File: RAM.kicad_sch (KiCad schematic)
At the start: 26 parts

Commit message: update traces
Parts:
- B5, B8, C10, C3, C4, C5, C6, C7, C8, C9, D10, D3, D4, D5, D6, D7, D8, D9, E10, E3, E4, E5, E6, E7, E8, E9: footprint Apple:DIP-16_W7.62mm -> Package_DIP:DIP-16_W7.62mm
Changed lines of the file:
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@@
       (effects (font (size 1.27 1.27)))
     )
-    (property "Footprint" "Apple:DIP-16_W7.62mm" (at 157.48 44.196 0)
+    (property "Footprint" "Package_DIP:DIP-16_W7.62mm" (at 157.48 44.196 0)
       (effects (font (size 1.27 1.27)) hide)
     )
@@
       (effects (font (size 1.27 1.27)))
     )
-    (property "Footprint" "Apple:DIP-16_W7.62mm" (at 189.992 44.196 0)
+    (property "Footprint" "Package_DIP:DIP-16_W7.62mm" (at 189.992 44.196 0)
       (effects (font (size 1.27 1.27)) hide)
     )
@@
       (effects (font (size 1.27 1.27)))
     )
-    (property "Footprint" "Apple:DIP-16_W7.62mm" (at 221.996 44.196 0)
+    (property "Footprint" "Package_DIP:DIP-16_W7.62mm" (at 221.996 44.196 0)
       (effects (font (size 1.27 1.27)) hide)
     )
@@
       (effects (font (size 1.27 1.27)))
     )
-    (property "Footprint" "Apple:DIP-16_W7.62mm" (at 319.786 44.196 0)
+    (property "Footprint" "Package_DIP:DIP-16_W7.62mm" (at 319.786 44.196 0)
       (effects (font (size 1.27 1.27)) hide)
     )
@@
       (effects (font (size 1.27 1.27)))
     )
-    (property "Footprint" "Apple:DIP-16_W7.62mm" (at 157.734 91.44 0)
+    (property "Footprint" "Package_DIP:DIP-16_W7.62mm" (at 157.734 91.44 0)
       (effects (font (size 1.27 1.27)) hide)
     )
@@
       (effects (font (size 1.27 1.27)))
     )
-    (property "Footprint" "Apple:DIP-16_W7.62mm" (at 190.246 91.44 0)
+    (property "Footprint" "Package_DIP:DIP-16_W7.62mm" (at 190.246 91.44 0)
       (effects (font (size 1.27 1.27)) hide)
     )
@@
       (effects (font (size 1.27 1.27)))
     )
-    (property "Footprint" "Apple:DIP-16_W7.62mm" (at 222.25 91.44 0)
+    (property "Footprint" "Package_DIP:DIP-16_W7.62mm" (at 222.25 91.44 0)
       (effects (font (size 1.27 1.27)) hide)
     )
@@
       (effects (font (size 1.27 1.27)))
     )
-    (property "Footprint" "Apple:DIP-16_W7.62mm" (at 287.528 91.44 0)
+    (property "Footprint" "Package_DIP:DIP-16_W7.62mm" (at 287.528 91.44 0)
       (effects (font (size 1.27 1.27)) hide)
     )
@@
       (effects (font (size 1.27 1.27)))
     )
-    (property "Footprint" "Apple:DIP-16_W7.62mm" (at 352.044 91.44 0)
+    (property "Footprint" "Package_DIP:DIP-16_W7.62mm" (at 352.044 91.44 0)
       (effects (font (size 1.27 1.27)) hide)
     )
@@
       (effects (font (size 1.27 1.27)))
     )
-    (property "Footprint" "Apple:DIP-16_W7.62mm" (at 125.73 44.45 0)
+    (property "Footprint" "Package_DIP:DIP-16_W7.62mm" (at 125.73 44.45 0)
       (effects (font (size 1.27 1.27)) hide)
     )
@@
       (effects (font (size 1.27 1.27)))
     )
-    (property "Footprint" "Apple:DIP-16_W7.62mm" (at 255.27 44.196 0)
+    (property "Footprint" "Package_DIP:DIP-16_W7.62mm" (at 255.27 44.196 0)
       (effects (font (size 1.27 1.27)) hide)
     )
@@
       (effects (font (size 1.27 1.27)))
     )
-    (property "Footprint" "Apple:DIP-16_W7.62mm" (at 287.274 44.196 0)
+    (property "Footprint" "Package_DIP:DIP-16_W7.62mm" (at 287.274 44.196 0)
       (effects (font (size 1.27 1.27)) hide)
     )
@@
       (effects (font (size 1.27 1.27)))
     )
-    (property "Footprint" "Apple:DIP-16_W7.62mm" (at 351.79 44.196 0)
+    (property "Footprint" "Package_DIP:DIP-16_W7.62mm" (at 351.79 44.196 0)
       (effects (font (size 1.27 1.27)) hide)
     )
@@
       (effects (font (size 1.27 1.27)))
     )
-    (property "Footprint" "Apple:DIP-16_W7.62mm" (at 255.524 91.44 0)
+    (property "Footprint" "Package_DIP:DIP-16_W7.62mm" (at 255.524 91.44 0)
       (effects (font (size 1.27 1.27)) hide)
     )
@@
       (effects (font (size 1.27 1.27)))
     )
-    (property "Footprint" "Apple:DIP-16_W7.62mm" (at 320.04 91.44 0)
+    (property "Footprint" "Package_DIP:DIP-16_W7.62mm" (at 320.04 91.44 0)
       (effects (font (size 1.27 1.27)) hide)
     )
@@
       (effects (font (size 1.27 1.27)))
     )
-    (property "Footprint" "Apple:DIP-16_W7.62mm" (at 123.952 139.192 0)
+    (property "Footprint" "Package_DIP:DIP-16_W7.62mm" (at 123.952 139.192 0)
       (effects (font (size 1.27 1.27)) hide)
     )
@@
       (effects (font (size 1.27 1.27)))
     )
-    (property "Footprint" "Apple:DIP-16_W7.62mm" (at 155.956 139.192 0)
+    (property "Footprint" "Package_DIP:DIP-16_W7.62mm" (at 155.956 139.192 0)
       (effects (font (size 1.27 1.27)) hide)
     )
@@
       (effects (font (size 1.27 1.27)))
     )
-    (property "Footprint" "Apple:DIP-16_W7.62mm" (at 188.468 139.192 0)
+    (property "Footprint" "Package_DIP:DIP-16_W7.62mm" (at 188.468 139.192 0)
       (effects (font (size 1.27 1.27)) hide)
     )
@@
       (effects (font (size 1.27 1.27)))
     )
-    (property "Footprint" "Apple:DIP-16_W7.62mm" (at 220.472 139.192 0)
+    (property "Footprint" "Package_DIP:DIP-16_W7.62mm" (at 220.472 139.192 0)
       (effects (font (size 1.27 1.27)) hide)
     )
@@
       (effects (font (size 1.27 1.27)))
     )
-    (property "Footprint" "Apple:DIP-16_W7.62mm" (at 253.746 139.192 0)
+    (property "Footprint" "Package_DIP:DIP-16_W7.62mm" (at 253.746 139.192 0)
       (effects (font (size 1.27 1.27)) hide)
     )
@@
       (effects (font (size 1.27 1.27)))
     )
-    (property "Footprint" "Apple:DIP-16_W7.62mm" (at 285.75 139.192 0)
+    (property "Footprint" "Package_DIP:DIP-16_W7.62mm" (at 285.75 139.192 0)
       (effects (font (size 1.27 1.27)) hide)
     )
@@
       (effects (font (size 1.27 1.27)))
     )
-    (property "Footprint" "Apple:DIP-16_W7.62mm" (at 318.262 139.192 0)
+    (property "Footprint" "Package_DIP:DIP-16_W7.62mm" (at 318.262 139.192 0)
       (effects (font (size 1.27 1.27)) hide)
     )
@@
       (effects (font (size 1.27 1.27)))
     )
-    (property "Footprint" "Apple:DIP-16_W7.62mm" (at 350.266 139.192 0)
+    (property "Footprint" "Package_DIP:DIP-16_W7.62mm" (at 350.266 139.192 0)
       (effects (font (size 1.27 1.27)) hide)
     )
@@
       (effects (font (size 1.27 1.27)))
     )
-    (property "Footprint" "Apple:DIP-16_W7.62mm" (at 96.52 218.44 0)
+    (property "Footprint" "Package_DIP:DIP-16_W7.62mm" (at 96.52 218.44 0)
       (effects (font (size 1.27 1.27)) hide)
     )
@@
       (effects (font (size 1.27 1.27)))
     )
-    (property "Footprint" "Apple:DIP-16_W7.62mm" (at 125.73 91.44 0)
+    (property "Footprint" "Package_DIP:DIP-16_W7.62mm" (at 125.73 91.44 0)
       (effects (font (size 1.27 1.27)) hide)
     )
@@
       (effects (font (size 1.27 1.27)))
     )
-    (property "Footprint" "Apple:DIP-16_W7.62mm" (at 160.02 218.44 0)
-      (effects (font (size 1.27 1.27)) hide)
-    )
+    (property "Footprint" "Package_DIP:DIP-16_W7.62mm" (at 160.02 218.44 0)
+      (effects (font (size 1.27 1.27)) hide)
+    )

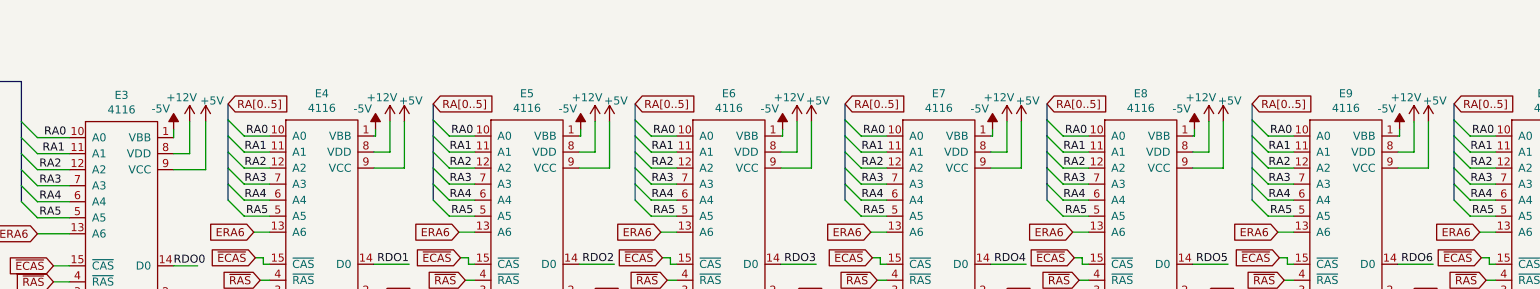
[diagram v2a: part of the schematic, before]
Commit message: more tracing - down to row E
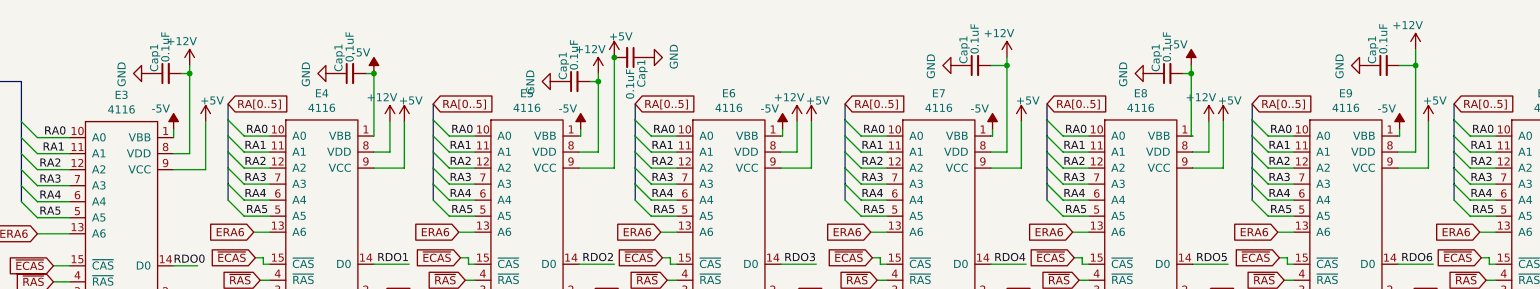
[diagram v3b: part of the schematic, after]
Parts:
- added Cap1 (x7): 0.1uF, Capacitor_THT:C_Disc_D5.0mm_W2.5mm_P5.00mm, symbol Device:C_Small
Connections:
- net +12V: now also Cap1.2, Cap1.2, Cap1.2, Cap1.2
- net +5V: now also Cap1.2
- net -5V: now also Cap1.2, Cap1.2
- net GND: now also Cap1.1, Cap1.1, Cap1.1, Cap1.1, Cap1.1, Cap1.1, Cap1.1

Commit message: more tracing
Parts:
- added Cap25, Cap26, Cap27, Cap28, Cap29, Cap30, Cap31: 0.1uF, Capacitor_THT:C_Disc_D5.0mm_W2.5mm_P5.00mm, symbol Device:C_Small
- renumbered Cap1 to Cap20, Cap1 to Cap21, Cap1 to Cap22, Cap1 to Cap23, Cap1 to Cap24, Cap1 to Cap3, Cap1 to Cap4
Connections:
- net +12V: now also Cap25.2, Cap28.2, Cap29.2, Cap31.2
- net +5V: now also Cap27.2
- net -5V: now also Cap26.2, Cap30.2
- net GND: now also Cap25.1, Cap26.1, Cap27.1, Cap28.1, Cap29.1, Cap30.1, Cap31.1

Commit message: finish tracing
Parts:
- added Cap34, Cap35, Cap36, Cap37, Cap38, Cap39, Cap40: 0.1uF, Capacitor_THT:C_Disc_D5.0mm_W2.5mm_P5.00mm, symbol Device:C_Small
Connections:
- net +12V: now also Cap34.2, Cap37.2, Cap38.2, Cap40.2
- net +5V: now also Cap35.2
- net -5V: now also Cap36.2, Cap39.2
- net GND: now also Cap34.1, Cap35.1, Cap36.1, Cap37.1, Cap38.1, Cap39.1, Cap40.1

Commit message: beautify resistors
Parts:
- Cap20, Cap21, Cap22, Cap23, Cap24, Cap25, Cap26, Cap27, Cap28, Cap29, Cap3, Cap30, Cap31, Cap34, Cap35, Cap36, Cap37, Cap38, Cap39, Cap4, Cap40: footprint Capacitor_THT:C_Disc_D5.0mm_W2.5mm_P5.00mm -> Apple-II:C_Disc_D5.0mm_W2.5mm_P5.00mm
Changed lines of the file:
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@@
       (effects (font (size 1.27 1.27)) (justify left))
     )
-    (property "Footprint" "Capacitor_THT:C_Disc_D5.0mm_W2.5mm_P5.00mm" (at 291.084 69.088 0)
+    (property "Footprint" "Apple-II:C_Disc_D5.0mm_W2.5mm_P5.00mm" (at 291.084 69.088 0)
       (effects (font (size 1.27 1.27)) hide)
     )
@@
       (effects (font (size 1.27 1.27)) (justify left))
     )
-    (property "Footprint" "Capacitor_THT:C_Disc_D5.0mm_W2.5mm_P5.00mm" (at 195.58 118.11 0)
+    (property "Footprint" "Apple-II:C_Disc_D5.0mm_W2.5mm_P5.00mm" (at 195.58 118.11 0)
       (effects (font (size 1.27 1.27)) hide)
     )
@@
       (effects (font (size 1.27 1.27)) (justify left))
     )
-    (property "Footprint" "Capacitor_THT:C_Disc_D5.0mm_W2.5mm_P5.00mm" (at 132.08 21.59 0)
+    (property "Footprint" "Apple-II:C_Disc_D5.0mm_W2.5mm_P5.00mm" (at 132.08 21.59 0)
       (effects (font (size 1.27 1.27)) hide)
     )
@@
       (effects (font (size 1.27 1.27)) (justify left))
     )
-    (property "Footprint" "Capacitor_THT:C_Disc_D5.0mm_W2.5mm_P5.00mm" (at 260.35 116.84 0)
+    (property "Footprint" "Apple-II:C_Disc_D5.0mm_W2.5mm_P5.00mm" (at 260.35 116.84 0)
       (effects (font (size 1.27 1.27)) hide)
     )
@@
       (effects (font (size 1.27 1.27)) (justify left))
     )
-    (property "Footprint" "Capacitor_THT:C_Disc_D5.0mm_W2.5mm_P5.00mm" (at 204.978 69.596 0)
+    (property "Footprint" "Apple-II:C_Disc_D5.0mm_W2.5mm_P5.00mm" (at 204.978 69.596 0)
       (effects (font (size 1.27 1.27)) hide)
     )
@@
       (effects (font (size 1.27 1.27)) (justify left))
     )
-    (property "Footprint" "Capacitor_THT:C_Disc_D5.0mm_W2.5mm_P5.00mm" (at 325.12 68.834 0)
+    (property "Footprint" "Apple-II:C_Disc_D5.0mm_W2.5mm_P5.00mm" (at 325.12 68.834 0)
       (effects (font (size 1.27 1.27)) hide)
     )
@@
       (effects (font (size 1.27 1.27)) (justify left))
     )
-    (property "Footprint" "Capacitor_THT:C_Disc_D5.0mm_W2.5mm_P5.00mm" (at 325.12 116.84 0)
+    (property "Footprint" "Apple-II:C_Disc_D5.0mm_W2.5mm_P5.00mm" (at 325.12 116.84 0)
       (effects (font (size 1.27 1.27)) hide)
     )
@@
       (effects (font (size 1.27 1.27)) (justify left))
     )
-    (property "Footprint" "Capacitor_THT:C_Disc_D5.0mm_W2.5mm_P5.00mm" (at 158.75 119.38 0)
+    (property "Footprint" "Apple-II:C_Disc_D5.0mm_W2.5mm_P5.00mm" (at 158.75 119.38 0)
       (effects (font (size 1.27 1.27)) hide)
     )
@@
       (effects (font (size 1.27 1.27)) (justify left))
     )
-    (property "Footprint" "Capacitor_THT:C_Disc_D5.0mm_W2.5mm_P5.00mm" (at 194.818 69.088 0)
+    (property "Footprint" "Apple-II:C_Disc_D5.0mm_W2.5mm_P5.00mm" (at 194.818 69.088 0)
       (effects (font (size 1.27 1.27)) hide)
     )
@@
       (effects (font (size 1.27 1.27)) (justify left))
     )
-    (property "Footprint" "Capacitor_THT:C_Disc_D5.0mm_W2.5mm_P5.00mm" (at 290.83 21.59 0)
+    (property "Footprint" "Apple-II:C_Disc_D5.0mm_W2.5mm_P5.00mm" (at 290.83 21.59 0)
       (effects (font (size 1.27 1.27)) hide)
     )
@@
       (effects (font (size 1.27 1.27)) (justify left))
     )
-    (property "Footprint" "Capacitor_THT:C_Disc_D5.0mm_W2.5mm_P5.00mm" (at 290.83 116.84 0)
+    (property "Footprint" "Apple-II:C_Disc_D5.0mm_W2.5mm_P5.00mm" (at 290.83 116.84 0)
       (effects (font (size 1.27 1.27)) hide)
     )
@@
       (effects (font (size 1.27 1.27)) (justify left))
     )
-    (property "Footprint" "Capacitor_THT:C_Disc_D5.0mm_W2.5mm_P5.00mm" (at 129.794 69.85 0)
+    (property "Footprint" "Apple-II:C_Disc_D5.0mm_W2.5mm_P5.00mm" (at 129.794 69.85 0)
       (effects (font (size 1.27 1.27)) hide)
     )
@@
       (effects (font (size 1.27 1.27)) (justify left))
     )
-    (property "Footprint" "Capacitor_THT:C_Disc_D5.0mm_W2.5mm_P5.00mm" (at 129.54 118.11 0)
+    (property "Footprint" "Apple-II:C_Disc_D5.0mm_W2.5mm_P5.00mm" (at 129.54 118.11 0)
       (effects (font (size 1.27 1.27)) hide)
     )
@@
       (effects (font (size 1.27 1.27)) (justify left))
     )
-    (property "Footprint" "Capacitor_THT:C_Disc_D5.0mm_W2.5mm_P5.00mm" (at 325.12 20.32 0)
+    (property "Footprint" "Apple-II:C_Disc_D5.0mm_W2.5mm_P5.00mm" (at 325.12 20.32 0)
       (effects (font (size 1.27 1.27)) hide)
     )
@@
       (effects (font (size 1.27 1.27)) (justify left))
     )
-    (property "Footprint" "Capacitor_THT:C_Disc_D5.0mm_W2.5mm_P5.00mm" (at 260.096 69.342 0)
+    (property "Footprint" "Apple-II:C_Disc_D5.0mm_W2.5mm_P5.00mm" (at 260.096 69.342 0)
       (effects (font (size 1.27 1.27)) hide)
     )
@@
       (effects (font (size 1.27 1.27)) (justify left))
     )
-    (property "Footprint" "Capacitor_THT:C_Disc_D5.0mm_W2.5mm_P5.00mm" (at 203.2 118.11 0)
+    (property "Footprint" "Apple-II:C_Disc_D5.0mm_W2.5mm_P5.00mm" (at 203.2 118.11 0)
       (effects (font (size 1.27 1.27)) hide)
     )
@@
       (effects (font (size 1.27 1.27)) (justify left))
     )
-    (property "Footprint" "Capacitor_THT:C_Disc_D5.0mm_W2.5mm_P5.00mm" (at 260.35 20.32 0)
+    (property "Footprint" "Apple-II:C_Disc_D5.0mm_W2.5mm_P5.00mm" (at 260.35 20.32 0)
       (effects (font (size 1.27 1.27)) hide)
     )
@@
       (effects (font (size 1.27 1.27)) (justify left))
     )
-    (property "Footprint" "Capacitor_THT:C_Disc_D5.0mm_W2.5mm_P5.00mm" (at 196.85 22.86 0)
+    (property "Footprint" "Apple-II:C_Disc_D5.0mm_W2.5mm_P5.00mm" (at 196.85 22.86 0)
       (effects (font (size 1.27 1.27)) hide)
     )
@@
       (effects (font (size 1.27 1.27)) (justify left))
     )
-    (property "Footprint" "Capacitor_THT:C_Disc_D5.0mm_W2.5mm_P5.00mm" (at 161.29 21.59 0)
+    (property "Footprint" "Apple-II:C_Disc_D5.0mm_W2.5mm_P5.00mm" (at 161.29 21.59 0)
       (effects (font (size 1.27 1.27)) hide)
     )
@@
       (effects (font (size 1.27 1.27)) (justify left))
     )
-    (property "Footprint" "Capacitor_THT:C_Disc_D5.0mm_W2.5mm_P5.00mm" (at 205.74 19.05 0)
+    (property "Footprint" "Apple-II:C_Disc_D5.0mm_W2.5mm_P5.00mm" (at 205.74 19.05 0)
       (effects (font (size 1.27 1.27)) hide)
     )
@@
       (effects (font (size 1.27 1.27)) (justify left))
     )
-    (property "Footprint" "Capacitor_THT:C_Disc_D5.0mm_W2.5mm_P5.00mm" (at 161.798 69.85 0)
-      (effects (font (size 1.27 1.27)) hide)
-    )
+    (property "Footprint" "Apple-II:C_Disc_D5.0mm_W2.5mm_P5.00mm" (at 161.798 69.85 0)
+      (effects (font (size 1.27 1.27)) hide)
+    )
